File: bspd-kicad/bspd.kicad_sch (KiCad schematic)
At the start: 23 parts

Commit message: work?
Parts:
- added U5: (no value), symbol bspd:TLV1704
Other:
- note added: "Fault: HIGH"
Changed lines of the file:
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@@
+		)
+	)
+	(text "Fault: HIGH\n"
+		(exclude_from_sim no)
+		(at 140.208 145.288 0)
+		(effects
+			(font
+				(size 1.27 1.27)
+			)
 		)
 	)
@@
 		)
 	)
+	(global_label "100ms_REF"
+		(shape input)
+		(at 181.61 58.42 180)
+		(fields_autoplaced yes)
+		(effects
+			(font
+				(size 1.27 1.27)
+			)
+			(justify right)
+		)
+		(property "Intersheetrefs" "${INTERSHEET_REFS}"
+			(at 167.7997 58.42 0)
+			(hide yes)
+			(show_name no)
+			(do_not_autoplace no)
+			(effects
+				(font
+					(size 1.27 1.27)
+				)
+				(justify right)
+			)
+		)
+	)
 	(global_label "TPS2_RAW"
 		(shape input)
@@
 		(property "Intersheetrefs" "${INTERSHEET_REFS}"
 			(at 15.5206 46.99 0)
+			(hide yes)
+			(show_name no)
+			(do_not_autoplace no)
+			(effects
+				(font
+					(size 1.27 1.27)
+				)
+				(justify right)
+			)
+		)
+	)
+	(global_label "100ms_REF"
+		(shape input)
+		(at 182.88 39.37 180)
+		(fields_autoplaced yes)
+		(effects
+			(font
+				(size 1.27 1.27)
+			)
+			(justify right)
+		)
+		(property "Intersheetrefs" "${INTERSHEET_REFS}"
+			(at 169.0697 39.37 0)
 			(hide yes)
 			(show_name no)
@@
 				)
 			)
+		)
+	)
+	(symbol
+		(lib_id "bspd:TLV1704")
+		(at 82.55 96.52 0)
+		(unit 1)
+		(body_style 1)
+		(exclude_from_sim no)
+		(in_bom yes)
+		(on_board yes)
+		(in_pos_files yes)
+		(dnp no)
+		(fields_autoplaced yes)
+		(property "Reference" "U5"
+			(at 100.33 92.6398 0)
+			(show_name no)
+			(do_not_autoplace no)
+			(effects
+				(font
+					(size 1.27 1.27)
+				)
+			)
+		)
+		(property "Value" ""
+			(at 82.55 96.52 0)
+			(show_name no)
+			(do_not_autoplace no)
+			(effects
+				(font
+					(size 1.27 1.27)
+				)
+			)
+		)
+		(property "Footprint" ""
+			(at 82.55 96.52 0)
+			(hide yes)
+			(show_name no)
+			(do_not_autoplace no)
+			(effects
+				(font
+					(size 1.27 1.27)
+				)
+			)
+		)
+		(property "Datasheet" ""
+			(at 82.55 96.52 0)
+			(hide yes)
+			(show_name no)
+			(do_not_autoplace no)
+			(effects
+				(font
+					(size 1.27 1.27)
+				)
+			)
+		)
+		(property "Description" ""
+			(at 82.55 96.52 0)
+			(hide yes)
+			(show_name no)
+			(do_not_autoplace no)
+			(effects
+				(font
+					(size 1.27 1.27)
+				)
+			)
+		)
+		(pin "12"
+		)
+		(pin "1"
+		)
+		(pin "10"
+		)
+		(pin "14"
+		)
+		(pin "5"
+		)
+		(pin "2"
+		)
+		(pin "13"
+		)
+		(pin "11"
+		)
+		(pin "8"
+		)
+		(pin "3"
+		)
+		(pin "7"
+		)
+		(pin "4"
+		)
+		(pin "9"
+		)
+		(pin "6"
+		)
+		(instances
+			(project "bspd"
+				(path "/e8b8835b-5dd0-46e2-9a0c-fed9bbaa86de"
+					(reference "U5")
+					(unit 1)
+				)
+			)

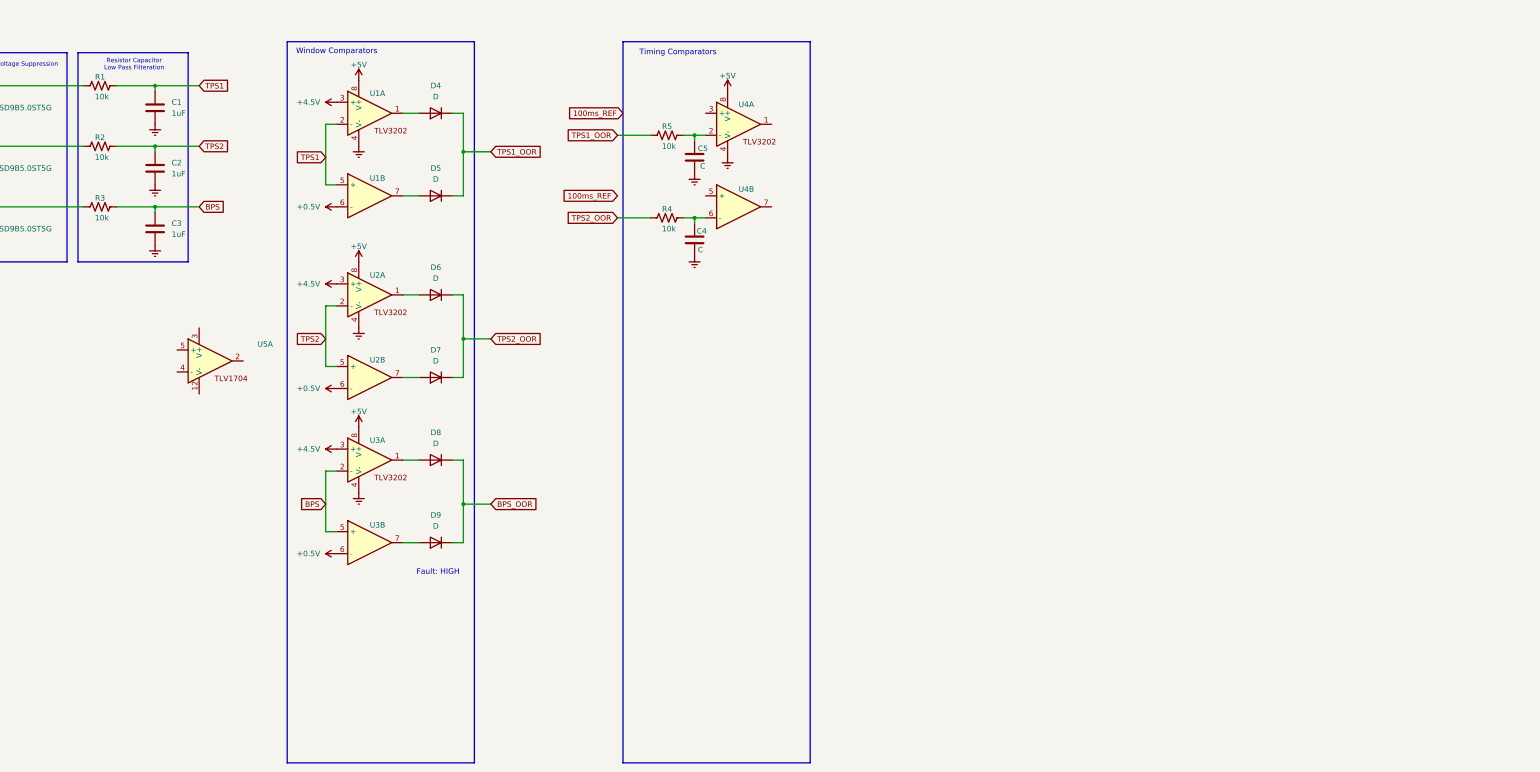
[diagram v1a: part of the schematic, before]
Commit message: Decided on TLV1704, working on HB and TP>10% logic
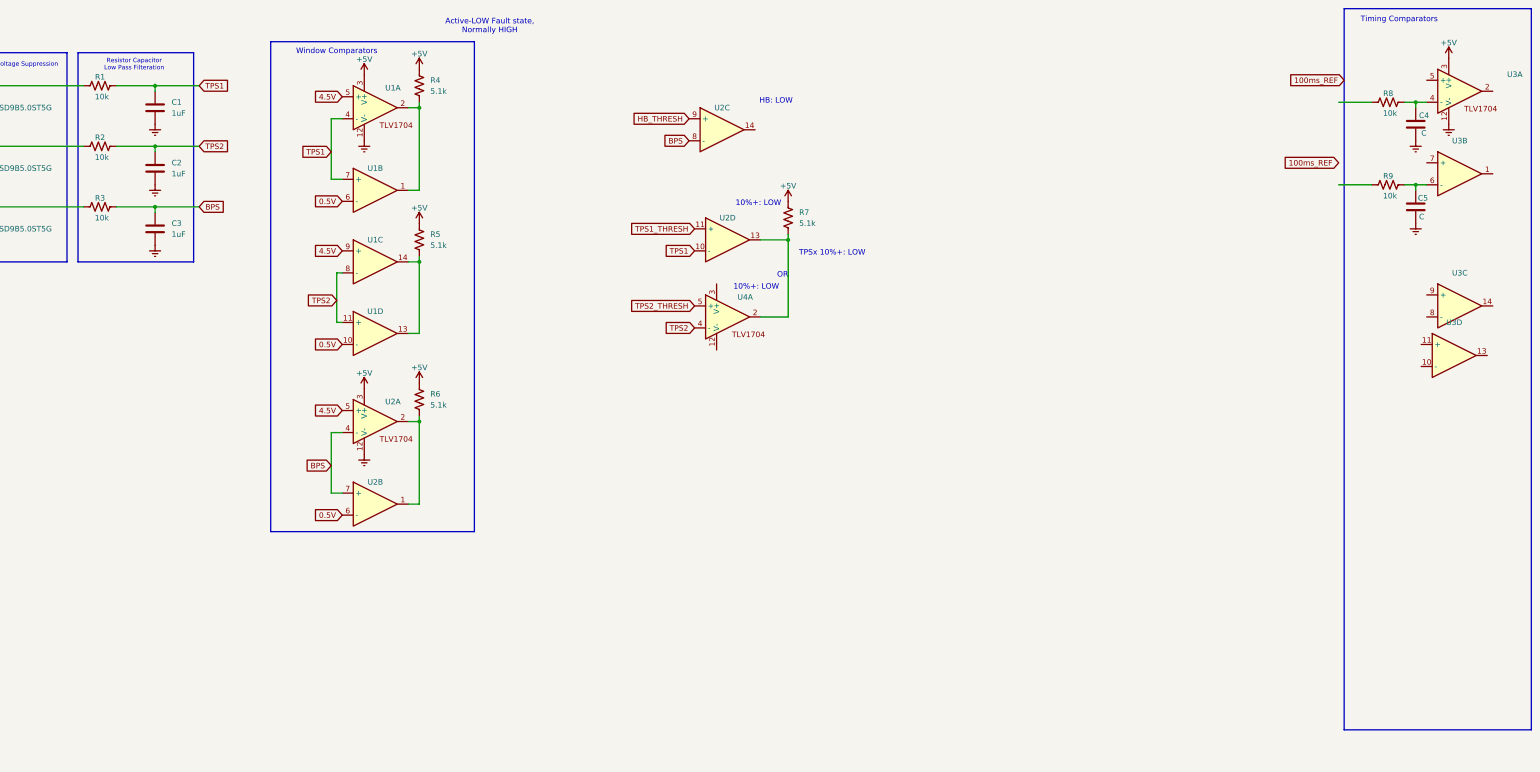
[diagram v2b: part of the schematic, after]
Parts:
- removed D4, D5, D6, D7, D8, D9: D, symbol Device:D
- removed U1, U2, U3, U4: (no value), bspd:TLV3202AQDGKRQ1, symbol bspd:TLV3202AIDGKR
- removed U5: (no value), symbol bspd:TLV1704
- added R4, R5, R6, R7: 5.1k, symbol Device:R_US
- added U1, U2, U3, U4: (no value), symbol bspd:TLV1704
- renumbered C5 to C4, C4 to C5, R5 to R8, R4 to R9
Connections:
- net +5V: now also R4.1, R5.1, R6.1, R7.1, U1.3 (V+), U2.3 (V+), U3.3 (V+)
- net BPS: now also U2.4 (-), U2.7 (+), U2.8 (-)
- net Earth: now also U1.12 (V-), U2.12 (V-), U3.12 (V-)
- net TPS1: now also U1.4 (-), U1.7 (+), U2.10 (-)
- net TPS2: now also U1.11 (+), U1.8 (-), U4.4 (-)
- net at C4.1, R8.2: now also U3.4 (-)
- net at C5.1, R9.2: now also U3.6 (-)
- net TPS1_OOR: no longer names the net of R8.1
- net TPS2_OOR: no longer names the net of R9.1
- new net: R5.2, U1.13, U1.14
- new net: R4.2, U1.1, U1.2
- new net: R7.2, U2.13, U4.2
- new net: R6.2, U2.1, U2.2
- new net 0.5V: U1.10 (-), U1.6 (-), U2.6 (-)
- new net 4.5V: U1.5 (+), U1.9 (+), U2.5 (+)
- new net HB_THRESH: U2.9 (+)
- new net TPS1_THRESH: U2.11 (+)
- new net TPS2_THRESH: U4.5 (+)
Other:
- note added: "10%+: LOW"
- note added: "Active-LOW Fault state, Normally HIGH"
- note added: "HB: LOW"
- note added: "OR"
- note added: "TPSx 10%+: LOW"
- note removed: "Fault: HIGH"
- moved on the sheet: C4, C5, R8, R9

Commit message: Completed timing
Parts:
- added C6, C7: 1uF, symbol Device:C
- added R10: 5.1k, symbol Device:R_US
- added R11, R12, R13, R14, R15, R16, R17, R18: 150k, symbol Device:R_US
- added unit 4 of U4
- C4: value C -> 5uF
- C5: value C -> 1uF
- R8, R9: value 10k -> 150k
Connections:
- net +5V: now also U4.3 (V+), R10.1
- net 0.5V: now also U3.8 (-)
- net BPS_RAW: now also R17.2
- net Earth: now also R8.1, U4.12 (V-), C6.2, C7.2, R16.1, R17.1
- net TPS1_RAW: now also R8.2
- net TPS2: now also U4.5 (+); no longer U4.4 (-)
- net TPS2_RAW: now also R16.2
- net TPS2_THRESH: now also U4.4 (-); no longer U4.5 (+)
- net +2V5: now reaches U3.10 (-)
- net +2V5: now also U3.4 (-), U3.6 (-), U4.10 (-)
- net at U3.11 (+): now also C6.1, R15.2
- net at U3.13: now also U3.1, U3.2, U4.13
- net TPS2_FAULT: now reaches R5.2, U1.13, U1.14
- net TPS2_FAULT: now also R15.1
- net TPS1_FAULT: now reaches R4.2, U1.1, U1.2
- net TPS1_FAULT: now also R9.1
- net at C5.1, R9.2: now also U3.7 (+); no longer U3.6 (-)
- net at R7.2, U2.13, U4.2: now also R12.2
- net HB&10%: now reaches U3.14
- net HB&10%: now also R13.1
- net at U3.9 (+): now also R11.1, R12.1
- net at U2.14: now also R10.2, R11.2
- net BPS_FAULT: now reaches R6.2, U2.1, U2.2
- net BPS_FAULT: now also R18.1
- net at U3.5 (+): now also C4.1, R14.2
- new net: C7.1, R18.2, U4.11 (+)
- new net: R13.2, R14.1
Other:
- note added: "HB&10% for more than 1sec: LOW"
- note added: "HB&10%: LOW"
- note added: "Hard Braking and Above 10% TPS"
- note added: "Note: swapped inputs due to TPS having different gradients"
- note added: "Open circuit pull down resistors"
- note added: "Out of Range: LOW Normally: HIGH"
- note added: "We expect low frequency noise"
- moved on the sheet: C1, C2, C3, R1, R2, R3, R4, R5, R6, R7, U1A, U1B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

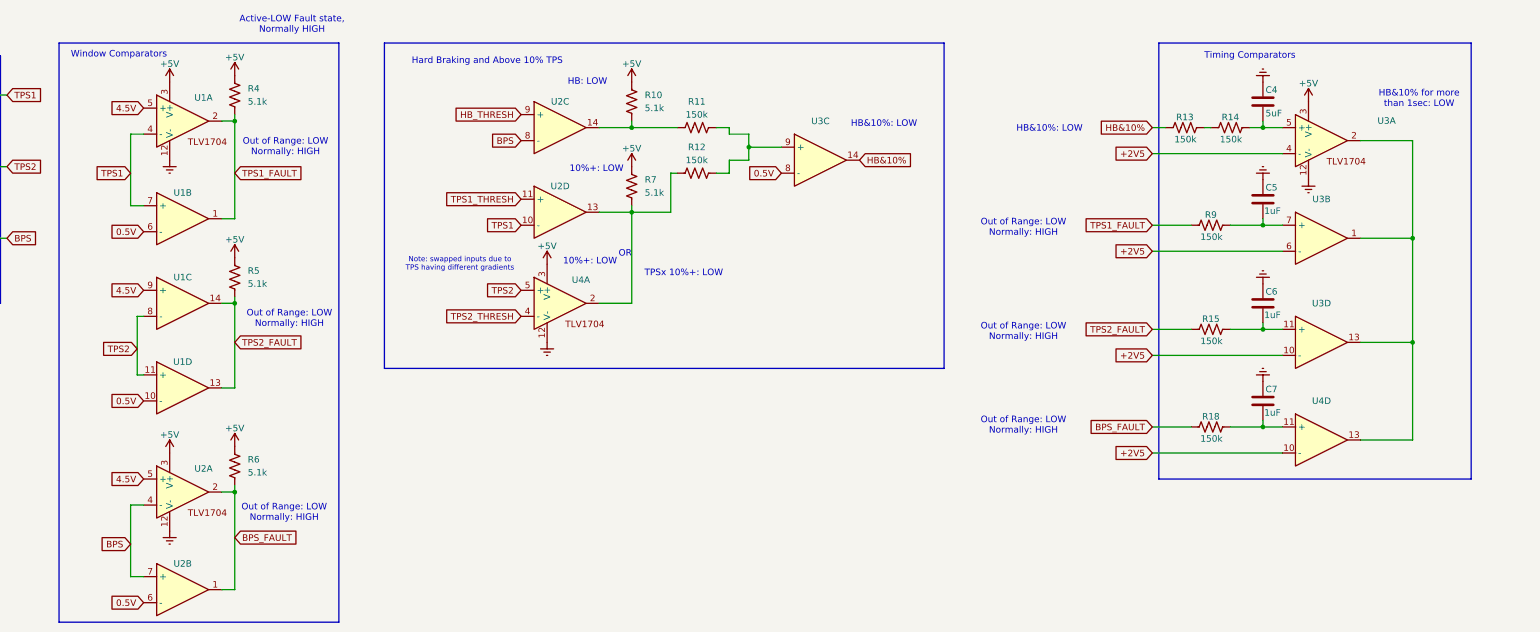
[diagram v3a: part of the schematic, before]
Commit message: Added fixed references
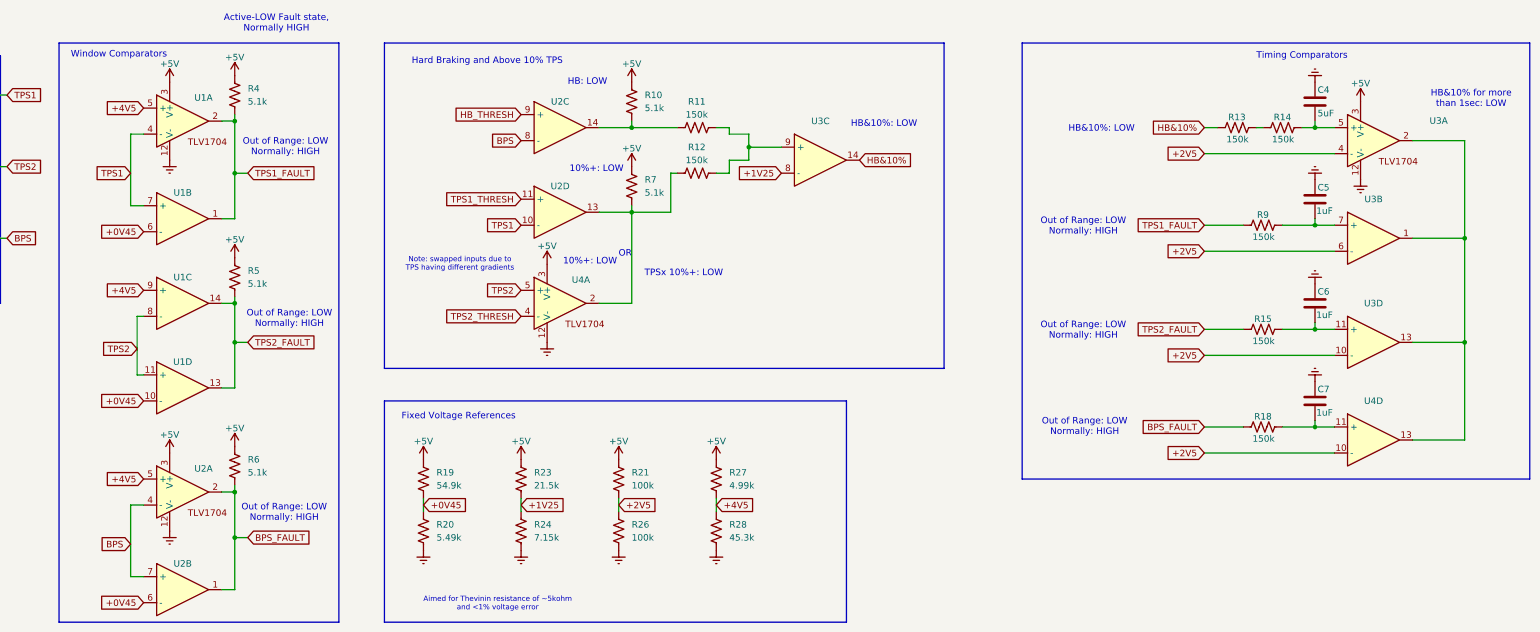
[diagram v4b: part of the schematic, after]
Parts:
- added R19: 54.9k, symbol Device:R_US
- added R20: 5.49k, symbol Device:R_US
- added R21, R26: 100k, symbol Device:R_US
- added R23: 21.5k, symbol Device:R_US
- added R24: 7.15k, symbol Device:R_US
- added R27: 4.99k, symbol Device:R_US
- added R28: 45.3k, symbol Device:R_US
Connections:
- net +2V5: now also R21.2, R26.1
- net +5V: now also R19.1, R21.1, R23.1, R27.1
- net Earth: now also R20.2, R24.2, R26.2, R28.2
- net 0.5V renamed +0V45
- net +0V45: now also R19.2, R20.1; no longer U3.8 (-)
- net 4.5V renamed +4V5
- net +4V5: now also R27.2, R28.1
- new net +1V25: R23.2, R24.1, U3.8 (-)
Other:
- note added: "Aimed for Thevinin resistance of ~5kohm and <1% voltage error"
- note added: "Fixed Voltage References"
- moved on the sheet: C4, C5, C6, C7, R13, R14, R15, R18, R9, U3A, U3B, U3D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

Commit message: Latching circuit done
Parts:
- added C8: xuF, symbol Device:C
- added D4: 1N4148W, Diode_SMD:D_SOD-123, symbol Diode:1N4148W
- added Q1: AO3400A, Package_TO_SOT_SMD:SOT-23, symbol Transistor_FET:AO3400A
- added R22, R25: 5.1k, symbol Device:R_US
- added R29: x, symbol Device:R_US
- added unit 3 of U4
- added unit 2 of U4
- added U6: SN74LVC2G00DCTR, bspd:SN74LVC2G00DCTR, symbol bspd:SN74LVC2G00DCTR
- added U8: SN74LVC3G14DCUR, bspd:SN74LVC3G14DCUR, symbol bspd:SN74LVC3G14DCUR
- U4: footprint (none) -> bspd:TLV1704
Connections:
- net +1V25: now also U3.6 (-); no longer U3.8 (-)
- net +2V5: now also U3.8 (-), U4.4 (-), U4.6 (-); no longer U3.4 (-), U3.6 (-), U4.10 (-)
- net +5V: now also U4.11 (+), D4.1 (K), R22.1, R25.1, R29.2, U4.9 (+), U6.8 (VCC), U8.8 (VCC)
- net Earth: now also U4.10 (-), C8.2, U4.8 (-), U6.4 (GND), U8.4 (GND)
- net HB&10%: now also U3.1, R22.2; no longer U3.14
- net TPS2: now also U3.5 (+); no longer U4.5 (+)
- net TPS2_THRESH: now also U3.4 (-); no longer U4.4 (-)
- net at C6.1, R15.2: now also U4.5 (+); no longer U3.11 (+)
- net at C7.1, R18.2: now also U4.7 (+); no longer U4.11 (+)
- net at C5.1, R9.2: now also U3.11 (+); no longer U3.7 (+)
- net at R12.2, R7.2, U2.13: now also U3.2; no longer U4.2
- net at R11.1, R12.1: now also U3.7 (+); no longer U3.9 (+)
- net at C4.1, R14.2: now also U3.9 (+); no longer U3.5 (+)
- new net: C8.1, D4.2 (A), R29.1, U8.3
- new net: U8.5, U8.6
- new net: U6.2 (B), U6.3 (Y)
- new net: Q1.1 (G), U6.5 (A), U6.7 (Y)
- new net: U6.6 (B), U8.2
- new net: U6.1 (A), U8.7
- new net +12V: Q1.3 (D)
- new net FAULT: R25.2, U3.13, U3.14, U4.1, U4.2, U8.1
- new net SC_OUT: Q1.2 (S)
- now unconnected: U4.13
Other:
- note added: "5V if no TPS and no HB (normal) 2.5V if one TPS and no HB (normal) 0V if one or both TPS and HB (fault)"
- note added: "BPS out of range for more than 100ms: LOW"
- note added: "Inverting to FAULT HIGH logic"
- note added: "Latching Circuit"
- note added: "Pulsed Power on Reset"
- note added: "R"
- note added: "S"
- note added: "SR Latch, Cross Coupled NAND"
- note added: "TPS1 out of range for more than 100ms: LOW"
- note added: "TPS2 out of range for more than 100ms: LOW"
- note added: "Unused"
- moved on the sheet: C4, C5, C6, C7, R13, R14, R15, R18, R9

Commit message: fixed foot print, added power and connector
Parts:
- added C1, C2: 1uF, Capacitor_SMD:C_0805_2012Metric_Pad1.18x1.45mm_HandSolder, symbol Device:C
- added J1: BSPD Connector, symbol Connector_Generic:Conn_02x03_Counter_Clockwise
- added U1: MCP1703T-5002E/CB, bspd:MCP1703T-5002E-CB, symbol bspd:MCP1703T-5002E-CB
- C10: renamed from C8; footprint (none) -> Capacitor_SMD:C_0805_2012Metric_Pad1.18x1.45mm_HandSolder
- C3: renamed from C4; footprint (none) -> Capacitor_SMD:C_0805_2012Metric_Pad1.18x1.45mm_HandSolder
- C4: renamed from C1; footprint (none) -> Capacitor_SMD:C_0805_2012Metric_Pad1.18x1.45mm_HandSolder
- C5: renamed from C2; footprint (none) -> Capacitor_SMD:C_0805_2012Metric_Pad1.18x1.45mm_HandSolder
- C6: renamed from C5; footprint (none) -> Capacitor_SMD:C_0805_2012Metric_Pad1.18x1.45mm_HandSolder
- C7: renamed from C3; footprint (none) -> Capacitor_SMD:C_0805_2012Metric_Pad1.18x1.45mm_HandSolder
- C8: renamed from C6; footprint (none) -> Capacitor_SMD:C_0805_2012Metric_Pad1.18x1.45mm_HandSolder
- C9: renamed from C7; footprint (none) -> Capacitor_SMD:C_0805_2012Metric_Pad1.18x1.45mm_HandSolder
- R1, R28, R29: footprint (none) -> Resistor_SMD:R_0805_2012Metric_Pad1.20x1.40mm_HandSolder
- R10: renamed from R2; footprint (none) -> Resistor_SMD:R_0805_2012Metric_Pad1.20x1.40mm_HandSolder
- R11: renamed from R12; footprint (none) -> Resistor_SMD:R_0805_2012Metric_Pad1.20x1.40mm_HandSolder
- R12: renamed from R16; footprint (none) -> Resistor_SMD:R_0805_2012Metric_Pad1.20x1.40mm_HandSolder
- R13: renamed from R7; footprint (none) -> Resistor_SMD:R_0805_2012Metric_Pad1.20x1.40mm_HandSolder
- R14: renamed from R9; footprint (none) -> Resistor_SMD:R_0805_2012Metric_Pad1.20x1.40mm_HandSolder
- R15: renamed from R3; footprint (none) -> Resistor_SMD:R_0805_2012Metric_Pad1.20x1.40mm_HandSolder
- R16: renamed from R17; footprint (none) -> Resistor_SMD:R_0805_2012Metric_Pad1.20x1.40mm_HandSolder
- R17: renamed from R5; footprint (none) -> Resistor_SMD:R_0805_2012Metric_Pad1.20x1.40mm_HandSolder
- R18: renamed from R15; footprint (none) -> Resistor_SMD:R_0805_2012Metric_Pad1.20x1.40mm_HandSolder
- R19: renamed from R18; footprint (none) -> Resistor_SMD:R_0805_2012Metric_Pad1.20x1.40mm_HandSolder
- R2: renamed from R4; footprint (none) -> Resistor_SMD:R_0805_2012Metric_Pad1.20x1.40mm_HandSolder
- R20: renamed from R6; footprint (none) -> Resistor_SMD:R_0805_2012Metric_Pad1.20x1.40mm_HandSolder
- R21: renamed from R19; footprint (none) -> Resistor_SMD:R_0805_2012Metric_Pad1.20x1.40mm_HandSolder
- R22: renamed from R23; footprint (none) -> Resistor_SMD:R_0805_2012Metric_Pad1.20x1.40mm_HandSolder
- R23: renamed from R21; footprint (none) -> Resistor_SMD:R_0805_2012Metric_Pad1.20x1.40mm_HandSolder
- R24: renamed from R27; footprint (none) -> Resistor_SMD:R_0805_2012Metric_Pad1.20x1.40mm_HandSolder
- R25: renamed from R20; footprint (none) -> Resistor_SMD:R_0805_2012Metric_Pad1.20x1.40mm_HandSolder
- R26: renamed from R24; footprint (none) -> Resistor_SMD:R_0805_2012Metric_Pad1.20x1.40mm_HandSolder
- R27: renamed from R26; footprint (none) -> Resistor_SMD:R_0805_2012Metric_Pad1.20x1.40mm_HandSolder
- R3: renamed from R10; footprint (none) -> Resistor_SMD:R_0805_2012Metric_Pad1.20x1.40mm_HandSolder
- R4: renamed from R8; footprint (none) -> Resistor_SMD:R_0805_2012Metric_Pad1.20x1.40mm_HandSolder
- R5: renamed from R25; footprint (none) -> Resistor_SMD:R_0805_2012Metric_Pad1.20x1.40mm_HandSolder
- R6: renamed from R11; footprint (none) -> Resistor_SMD:R_0805_2012Metric_Pad1.20x1.40mm_HandSolder
- R7: renamed from R13; footprint (none) -> Resistor_SMD:R_0805_2012Metric_Pad1.20x1.40mm_HandSolder
- R8: renamed from R14; footprint (none) -> Resistor_SMD:R_0805_2012Metric_Pad1.20x1.40mm_HandSolder
- R9: renamed from R22; footprint (none) -> Resistor_SMD:R_0805_2012Metric_Pad1.20x1.40mm_HandSolder
- U2: renamed from U1; footprint (none) -> bspd:TLV1704
- U3: renamed from U2; footprint (none) -> bspd:TLV1704
- U4: renamed from U3; footprint (none) -> bspd:TLV1704
- renumbered U4 to U5, U8 to U6, U6 to U7
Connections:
- net +12V: now also C1.2, J1.1 (Pin_1), U1.3 (VIN)
- net +5V: now also C2.2, U1.2 (VOUT)
- net BPS_RAW: now also J1.4 (Pin_4)
- net Earth: now also C1.1, C2.1, J1.3 (Pin_3), U1.1 (GND)
- net SC_OUT: now also J1.2 (Pin_2)
- net TPS1_RAW: now also J1.6 (Pin_6)
- net TPS2_RAW: now also J1.5 (Pin_5)
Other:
- note added: "12V to 5V Converter"
- note added: "BSPD Connector"
- note added: "Single Pulsed Power on Reset"
- note removed: "Pulsed Power on Reset"
- moved on the sheet: C10, C3, C4, C5, C6, C7, C8, C9, D1, D2, D3, D4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

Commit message: Begun layout
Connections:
- net +2V5: now also U5.10 (-), U5.8 (-); no longer U4.10 (-), U4.8 (-)
- net +5V: now also U4.11 (+), U4.9 (+); no longer U5.11 (+), U5.9 (+)
- net Earth: now also U4.10 (-), U4.8 (-); no longer U5.10 (-), U5.8 (-)
- net FAULT: now also U5.13, U5.14; no longer U4.13, U4.14
- net at C9.1, R19.2: now also U5.11 (+); no longer U5.7 (+)
- net at C6.1, R14.2: now also U5.7 (+); no longer U4.11 (+)
- net at C3.1, R8.2: now also U5.5 (+); no longer U4.9 (+)
- net at C8.1, R18.2: now also U5.9 (+); no longer U5.5 (+)
